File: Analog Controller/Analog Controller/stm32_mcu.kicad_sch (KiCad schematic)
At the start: 0 parts

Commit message: Completed Analog Controller Board
Completed Analog Controller Board schematic and pcb layout :)
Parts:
- added C1, C20: 100n, Resistor_SMD:R_0603_1608Metric_Pad0.98x0.95mm_HandSolder, symbol Device:C_Small
- added C19, C3: 1u, Resistor_SMD:R_0603_1608Metric_Pad0.98x0.95mm_HandSolder, symbol Device:C_Small
- added C2: 10n, Resistor_SMD:R_0603_1608Metric_Pad0.98x0.95mm_HandSolder, symbol Device:C_Small
- added J5: Conn_01x04, Connector_PinSocket_2.54mm:PinSocket_1x04_P2.54mm_Vertical, symbol Connector_Generic:Conn_01x04
- added J9: 284697-E, 284697-E:284697E, symbol 284697-E:284697-E
- added R10, R9: 4.7k, Resistor_SMD:R_0603_1608Metric_Pad0.98x0.95mm_HandSolder, symbol Device:R_US
- added SW2: SW_Omron_B3FS, Button_Switch_SMD:SW_SPST_Omron_B3FS-101xP, symbol Switch:SW_Omron_B3FS
- added U10: TCA9535DBR, Package_SO:SSOP-24_5.3x8.2mm_P0.65mm, symbol Interface_Expansion:TCA9535DBR
- added U9: STM8L152K4T6, STM8L152K4T6:LQFP-32, symbol STM8L152K4T6:STM8L152K4T6
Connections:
- net CS_0: now also U10.4 (P00)
- net CS_1: now also U10.5 (P01)
- net CS_2: now also U10.6 (P02)
- net CS_3: now also U10.7 (P03)
- net CS_4: now also U10.8 (P04)
- net CS_5: now also U10.9 (P05)
- net CS_6: now also U10.10 (P06)
- net CS_7: now also U10.11 (P07)
- net CS_8: now also U10.13 (P10)
- net MOSI: now also U9.19 (PB6)
- net POT_ADC_0: now also U9.6 (PA6)
- net POT_ADC_1: now also U9.5 (PA5)
- net POT_ADC_2: now also U9.4 (PA4)
- net SPI_CLK: now also U9.18 (PB5)
- new net +3V3: C1.1, C19.1, C2.1, C20.1, C3.1, J9.1, R10.1, R9.1, U10.24 (VCC), U9.8 (VDD1/VDDA/VREF+), U9.9 (VLCD)
- new net CS_10: U10.15 (P12)
- new net CS_11: U10.16 (P13)
- new net CS_9: U10.14 (P11)
- new net Effect_Select_0: U9.12 (PD3)
- new net Effect_Select_1: U9.11 (PD2)
- new net GND: C1.2, C19.2, C2.2, C20.2, C3.2, J5.3 (Pin_3), J5.4 (Pin_4), J9.3, J9.5 (MP1), J9.6 (MP2), J9.7 (MP3), J9.8 (MP4), SW2.1, U10.12 (GND), U10.2 (A1), U10.21 (A0), U10.3 (A2), U9.7 (VSS1/VSSA/VREF-)
- new net I2C_SCL: R10.2, U10.22 (SCL), U9.26 (PC1)
- new net I2C_SDA: R9.2, U10.23 (SDA), U9.25 (PC0)
- new net LED_0: U10.17 (P14)
- new net LED_1: U10.18 (P15)
- new net LED_2: U10.19 (P16)
- new net RST: J9.4, SW2.2, U9.1 (NRST/PA1)
- new net SPDT_IO_0: U9.17 (PB4)
- new net SPDT_IO_1: U9.21 (PD4)
- new net SPDT_IO_2: U9.16 (PB3)
- new net SPDT_IO_3: U9.15 (PB2)
- new net SPDT_IO_4: U9.14 (PB1)
- new net SPDT_IO_5: U9.13 (PB0)
- new net SWIM: J9.2, U9.32 (PA0)
- new net Toggle_ON/OFF: U9.10 (PD1)
- new net UART_RX: J5.1 (Pin_1), U9.27 (PC2)
- new net UART_TX: J5.2 (Pin_2), U9.28 (PC3)
- no-connect marks 0 -> 11

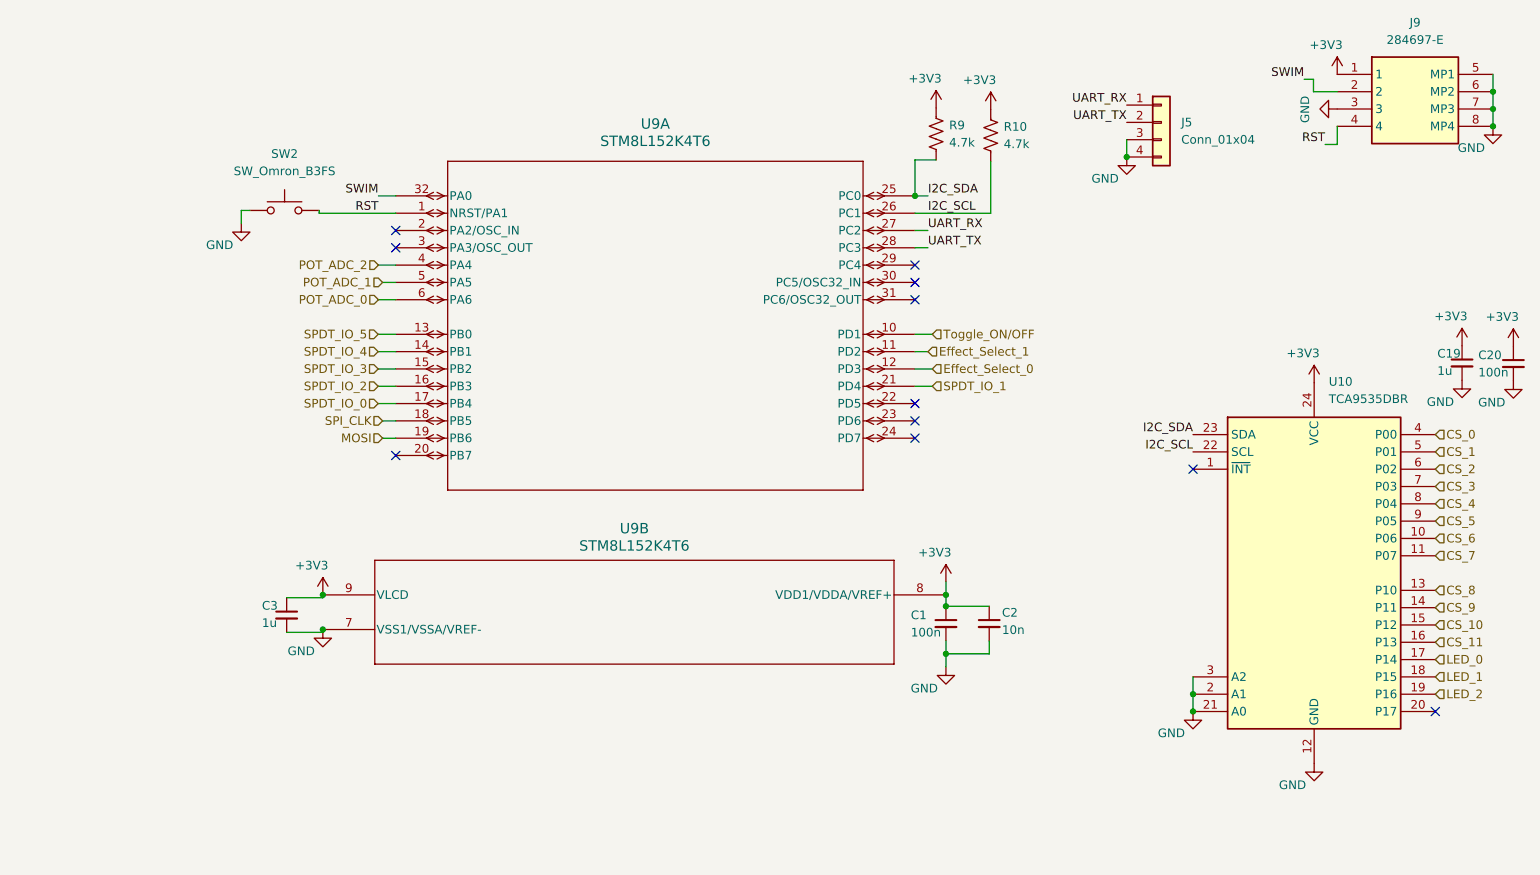
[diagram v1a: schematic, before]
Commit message: Added new stm32 microcontroller, redid pcb layout
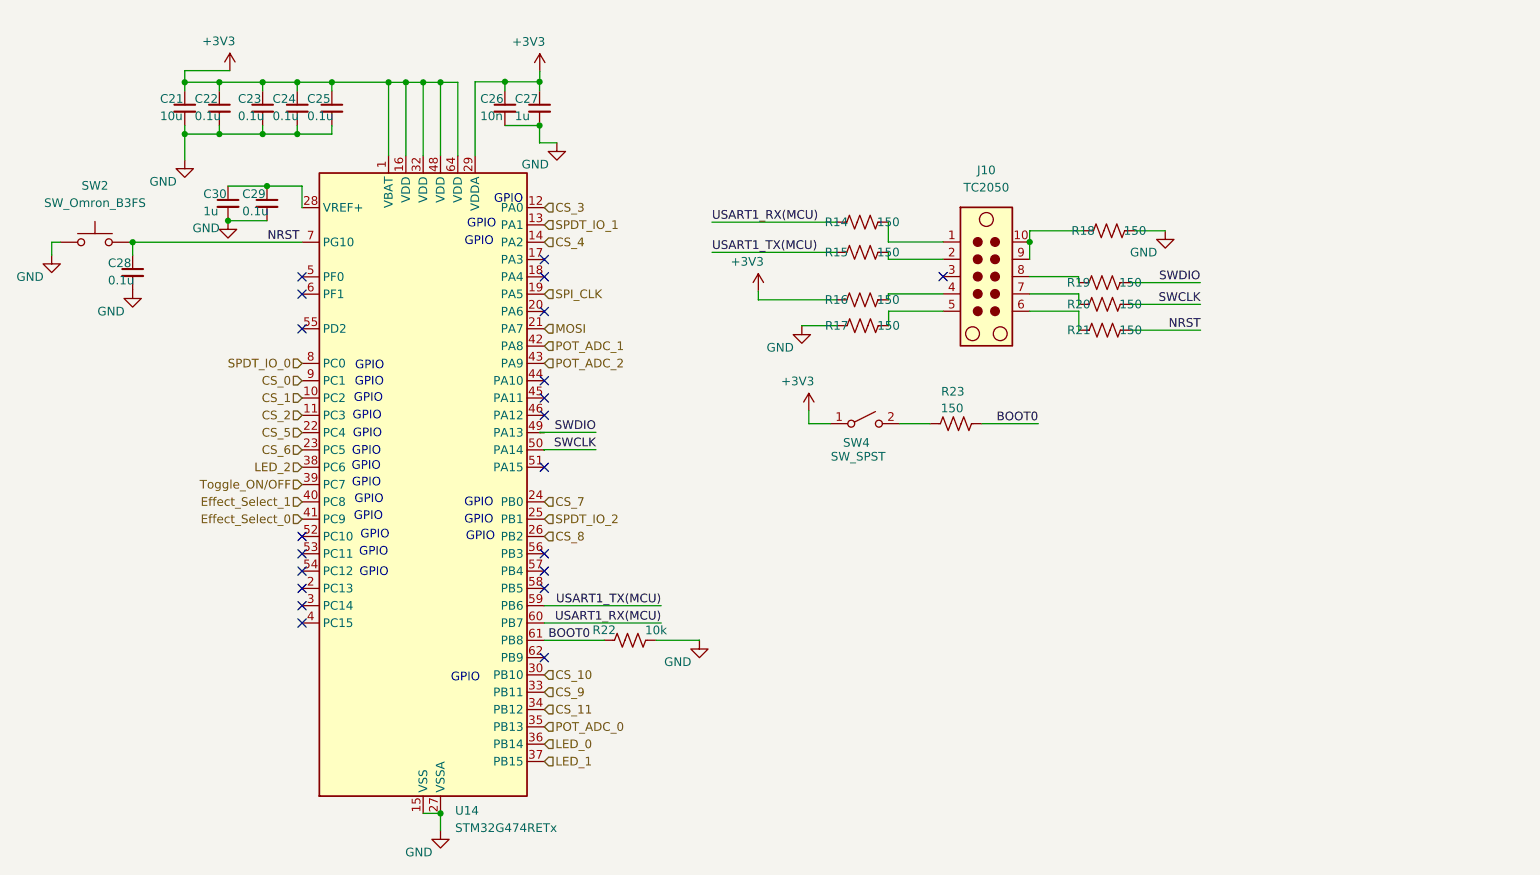
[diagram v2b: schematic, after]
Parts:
- removed C1, C20: 100n, Resistor_SMD:R_0603_1608Metric_Pad0.98x0.95mm_HandSolder, symbol Device:C_Small
- removed C19, C3: 1u, Resistor_SMD:R_0603_1608Metric_Pad0.98x0.95mm_HandSolder, symbol Device:C_Small
- removed C2: 10n, Resistor_SMD:R_0603_1608Metric_Pad0.98x0.95mm_HandSolder, symbol Device:C_Small
- removed J5: Conn_01x04, Connector_PinSocket_2.54mm:PinSocket_1x04_P2.54mm_Vertical, symbol Connector_Generic:Conn_01x04
- removed J9: 284697-E, 284697-E:284697E, symbol 284697-E:284697-E
- removed R10, R9: 4.7k, Resistor_SMD:R_0603_1608Metric_Pad0.98x0.95mm_HandSolder, symbol Device:R_US
- removed U10: TCA9535DBR, Package_SO:SSOP-24_5.3x8.2mm_P0.65mm, symbol Interface_Expansion:TCA9535DBR
- removed U9: STM8L152K4T6, STM8L152K4T6:LQFP-32, symbol STM8L152K4T6:STM8L152K4T6
- added C21: 10u, Resistor_SMD:R_0603_1608Metric_Pad0.98x0.95mm_HandSolder, symbol Device:C_Small
- added C22, C23, C24, C25, C28, C29: 0.1u, Resistor_SMD:R_0603_1608Metric_Pad0.98x0.95mm_HandSolder, symbol Device:C_Small
- added C26: 10n, Resistor_SMD:R_0603_1608Metric_Pad0.98x0.95mm_HandSolder, symbol Device:C_Small
- added C27, C30: 1u, Resistor_SMD:R_0603_1608Metric_Pad0.98x0.95mm_HandSolder, symbol Device:C_Small
- added J10: TC2050, Connector:Tag-Connect_TC2050-IDC-FP_2x05_P1.27mm_Vertical, symbol Connector:TC2050
- added R14, R15, R16, R17, R18, R19, R20, R21, R23: 150, Resistor_SMD:R_0603_1608Metric_Pad0.98x0.95mm_HandSolder, symbol Device:R_US
- added R22: 10k, Resistor_SMD:R_0603_1608Metric_Pad0.98x0.95mm_HandSolder, symbol Device:R_US
- added SW4: SW_SPST, Button_Switch_SMD:SW_SPST_B3U-1000P, symbol Switch:SW_SPST
- added U14: STM32G474RETx, Package_QFP:LQFP-64_10x10mm_P0.5mm, symbol MCU_ST_STM32G4:STM32G474RETx
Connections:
- net +3V3: now also C21.1, C22.1, C23.1, C24.1, C25.1, C26.1, C27.1, R16.1, SW4.1 (A), U14.1 (VBAT), U14.16 (VDD), U14.29 (VDDA), U14.32 (VDD), U14.48 (VDD), U14.64 (VDD)
- net CS_0: now also U14.9 (PC1)
- net CS_1: now also U14.10 (PC2)
- net CS_10: now also U14.30 (PB10)
- net CS_11: now also U14.34 (PB12)
- net CS_2: now also U14.11 (PC3)
- net CS_3: now also U14.12 (PA0)
- net CS_4: now also U14.14 (PA2)
- net CS_5: now also U14.22 (PC4)
- net CS_6: now also U14.23 (PC5)
- net CS_7: now also U14.24 (PB0)
- net CS_8: now also U14.26 (PB2)
- net CS_9: now also U14.33 (PB11)
- net Effect_Select_0: now also U14.41 (PC9)
- net Effect_Select_1: now also U14.40 (PC8)
- net GND: now also C21.2, C22.2, C23.2, C24.2, C25.2, C26.2, C27.2, C28.2, C29.2, C30.2, R17.1, R18.2, R22.1, U14.15 (VSS), U14.27 (VSSA), U14.31 (VSS), U14.47 (VSS), U14.63 (VSS)
- net LED_0: now also U14.36 (PB14)
- net LED_1: now also U14.37 (PB15)
- net LED_2: now also U14.38 (PC6)
- net MOSI: now also U14.21 (PA7)
- net POT_ADC_0: now also U14.35 (PB13)
- net POT_ADC_1: now also U14.42 (PA8)
- net POT_ADC_2: now also U14.43 (PA9)
- net SPDT_IO_0: now also U14.8 (PC0)
- net SPDT_IO_1: now also U14.13 (PA1)
- net SPDT_IO_2: now also U14.25 (PB1)
- net SPI_CLK: now also U14.19 (PA5)
- net Toggle_ON/OFF: now also U14.39 (PC7)
- net RST renamed NRST
- net NRST: now also C28.1, R21.2, U14.7 (PG10)
- new net: J10.1, R14.2
- new net: J10.10, J10.9, R18.1
- new net: J10.2, R15.2
- new net: J10.4, R16.2
- new net: J10.5, R17.2
- new net: J10.6, R21.1
- new net: J10.7, R20.1
- new net: J10.8, R19.1
- new net: C29.1, C30.1, U14.28 (VREF+)
- new net: R23.1, SW4.2 (B)
- new net BOOT0: R22.2, R23.2, U14.61 (PB8)
- new net SWCLK: R20.2, U14.50 (PA14)
- new net SWDIO: R19.2, U14.49 (PA13)
- new net USART1_RX(MCU): R14.1, U14.60 (PB7)
- new net USART1_TX(MCU): R15.1, U14.59 (PB6)
- no-connect marks 11 -> 21
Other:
- note added: "GPIO"
- moved on the sheet: SW2
